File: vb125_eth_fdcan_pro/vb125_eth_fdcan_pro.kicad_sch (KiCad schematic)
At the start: 0 parts

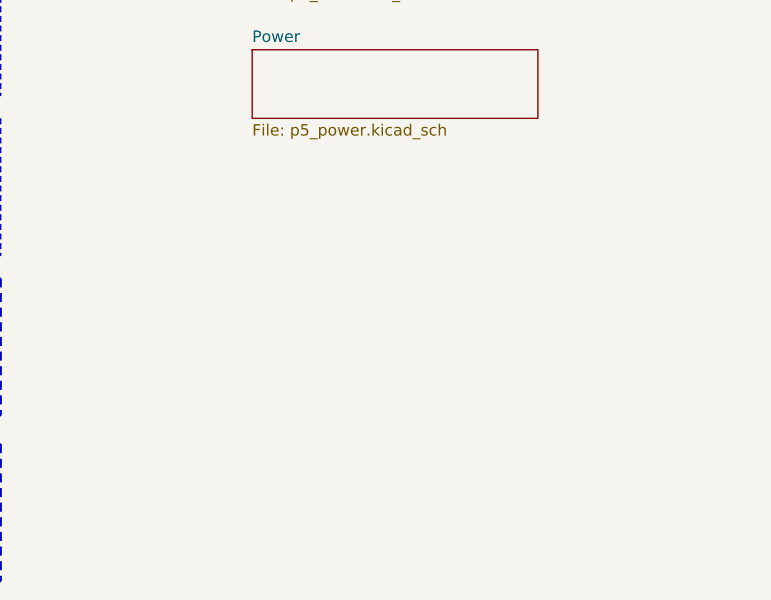
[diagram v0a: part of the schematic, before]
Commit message: AOZ schematic. 3V3 DC-DC. Partly bus power.
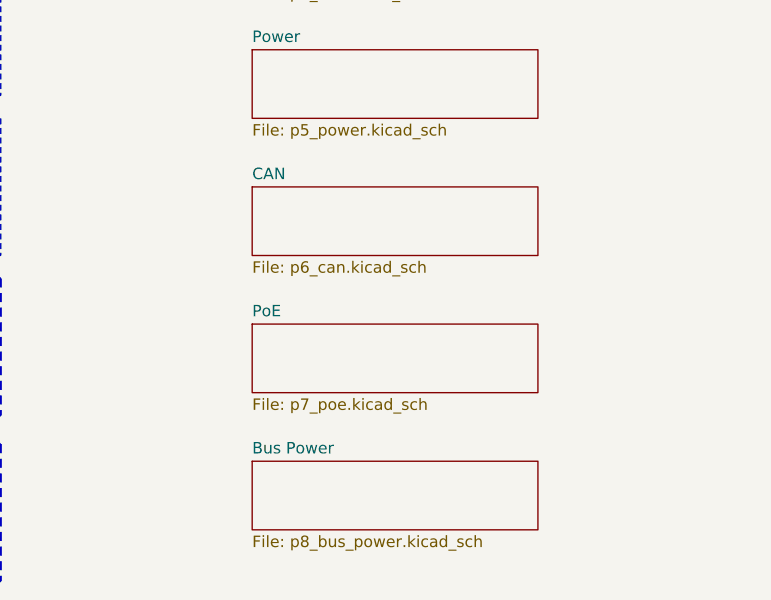
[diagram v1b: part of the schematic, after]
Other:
- added sheet Bus Power (p8_bus_power.kicad_sch)
- added sheet CAN (p6_can.kicad_sch)
- added sheet PoE (p7_poe.kicad_sch)
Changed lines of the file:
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@@
+    )
+  )
+  (sheet (at 69.85 180.34) (size 31.75 7.62) (fields_autoplaced)
+    (stroke (width 0.1524) (type solid))
+    (fill (color 0 0 0 0.0000))
+    (property "Sheetname" "Bus Power" (at 69.85 179.6284 0)
+      (effects (font (size 1.27 1.27)) (justify left bottom))
+    )
+    (property "Sheetfile" "p8_bus_power.kicad_sch" (at 69.85 188.5446 0)
+      (effects (font (size 1.27 1.27)) (justify left top))
+    )
+    (instances
+      (project "vb125_eth_fdcan_pro"
+        (path "/b473bccb-f14c-41d5-b473-137d3ef8ae1e" (page "8"))
+      )
     )
   )
@@
     )
   )
+  (sheet (at 69.85 165.1) (size 31.75 7.62) (fields_autoplaced)
+    (stroke (width 0.1524) (type solid))
+    (fill (color 0 0 0 0.0000))
+    (property "Sheetname" "PoE" (at 69.85 164.3884 0)
+      (effects (font (size 1.27 1.27)) (justify left bottom))
+    )
+    (property "Sheetfile" "p7_poe.kicad_sch" (at 69.85 173.3046 0)
+      (effects (font (size 1.27 1.27)) (justify left top))
+    )
+    (instances
+      (project "vb125_eth_fdcan_pro"
+        (path "/b473bccb-f14c-41d5-b473-137d3ef8ae1e" (page "7"))
+      )
+    )
+  )
   (sheet (at 69.85 104.14) (size 31.75 7.62) (fields_autoplaced)
     (stroke (width 0.1524) (type solid))
@@
       )
     )
+  )
+  (sheet (at 69.85 149.86) (size 31.75 7.62) (fields_autoplaced)
+    (stroke (width 0.1524) (type solid))
+    (fill (color 0 0 0 0.0000))
+    (property "Sheetname" "CAN" (at 69.85 149.1484 0)
+      (effects (font (size 1.27 1.27)) (justify left bottom))
+    )
+    (property "Sheetfile" "p6_can.kicad_sch" (at 69.85 158.0646 0)
+      (effects (font (size 1.27 1.27)) (justify left top))
+    )
+    (instances
+      (project "vb125_eth_fdcan_pro"
+        (path "/b473bccb-f14c-41d5-b473-137d3ef8ae1e" (page "6"))
+      )
+    )

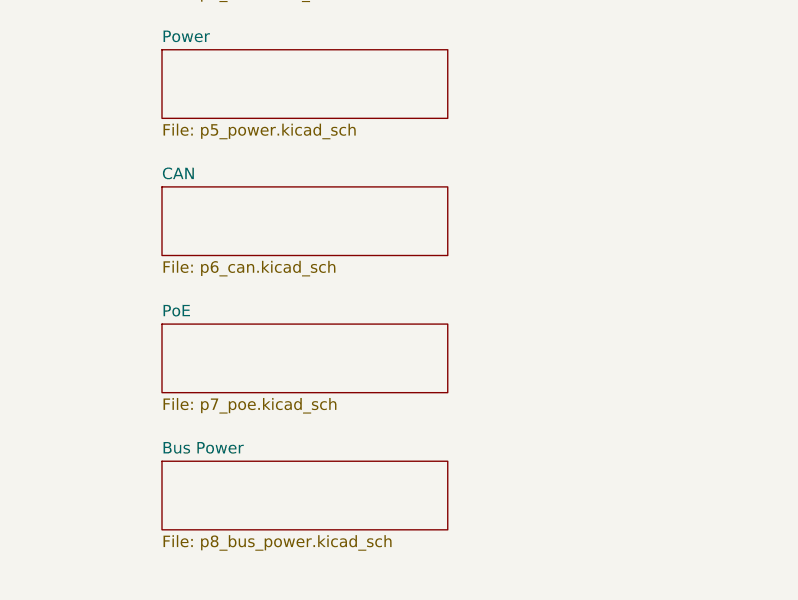
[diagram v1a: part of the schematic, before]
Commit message: Work on PoE. Rearrange pages.
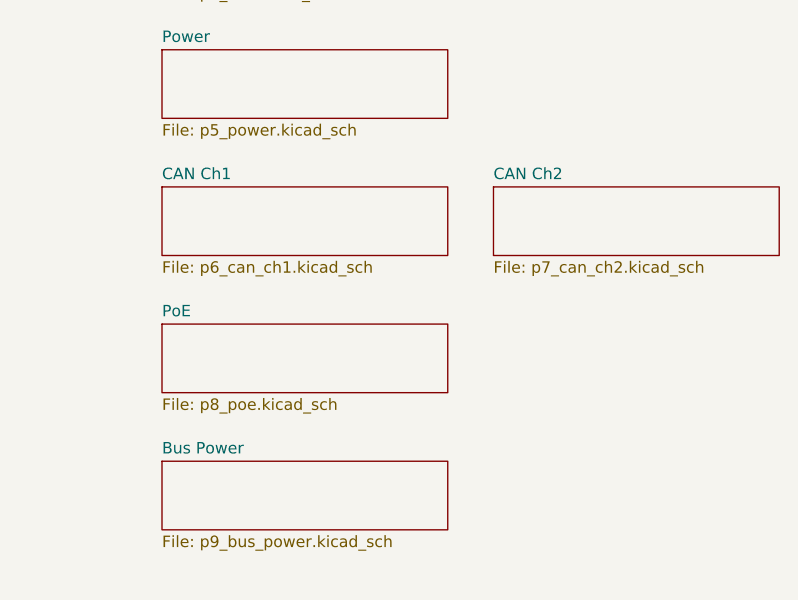
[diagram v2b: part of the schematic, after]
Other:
- sheet CAN renamed CAN Ch1
- added sheet CAN Ch2 (p7_can_ch2.kicad_sch)
- sheet Bus Power: file p8_bus_power.kicad_sch -> p9_bus_power.kicad_sch
- sheet CAN Ch1: file p6_can.kicad_sch -> p6_can_ch1.kicad_sch
- sheet PoE: file p7_poe.kicad_sch -> p8_poe.kicad_sch
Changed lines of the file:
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@@
       (effects (font (size 1.27 1.27)) (justify left bottom))
     )
-    (property "Sheetfile" "p8_bus_power.kicad_sch" (at 69.85 188.5446 0)
+    (property "Sheetfile" "p9_bus_power.kicad_sch" (at 69.85 188.5446 0)
       (effects (font (size 1.27 1.27)) (justify left top))
     )
     (instances
       (project "vb125_eth_fdcan_pro"
-        (path "/b473bccb-f14c-41d5-b473-137d3ef8ae1e" (page "8"))
+        (path "/b473bccb-f14c-41d5-b473-137d3ef8ae1e" (page "9"))
       )
     )
@@
       (effects (font (size 1.27 1.27)) (justify left bottom))
     )
-    (property "Sheetfile" "p7_poe.kicad_sch" (at 69.85 173.3046 0)
+    (property "Sheetfile" "p8_poe.kicad_sch" (at 69.85 173.3046 0)
       (effects (font (size 1.27 1.27)) (justify left top))
     )
     (instances
       (project "vb125_eth_fdcan_pro"
-        (path "/b473bccb-f14c-41d5-b473-137d3ef8ae1e" (page "7"))
+        (path "/b473bccb-f14c-41d5-b473-137d3ef8ae1e" (page "8"))
       )
     )
@@
     (stroke (width 0.1524) (type solid))
     (fill (color 0 0 0 0.0000))
-    (property "Sheetname" "CAN" (at 69.85 149.1484 0)
+    (property "Sheetname" "CAN Ch1" (at 69.85 149.1484 0)
       (effects (font (size 1.27 1.27)) (justify left bottom))
     )
-    (property "Sheetfile" "p6_can.kicad_sch" (at 69.85 158.0646 0)
+    (property "Sheetfile" "p6_can_ch1.kicad_sch" (at 69.85 158.0646 0)
       (effects (font (size 1.27 1.27)) (justify left top))
     )
@@
       )
     )
+  )
+  (sheet (at 106.68 149.86) (size 31.75 7.62) (fields_autoplaced)
+    (stroke (width 0.1524) (type solid))
+    (fill (color 0 0 0 0.0000))
+    (property "Sheetname" "CAN Ch2" (at 106.68 149.1484 0)
+      (effects (font (size 1.27 1.27)) (justify left bottom))
+    )
+    (property "Sheetfile" "p7_can_ch2.kicad_sch" (at 106.68 158.0646 0)
+      (effects (font (size 1.27 1.27)) (justify left top))
+    )
+    (instances
+      (project "vb125_eth_fdcan_pro"
+        (path "/b473bccb-f14c-41d5-b473-137d3ef8ae1e" (page "7"))
+      )
+    )
